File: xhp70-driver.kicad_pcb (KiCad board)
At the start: 2 copper layers, 65 x 39 mm, 13 parts, among them Q1 Q_NMOS_GDS, U1 AL8871Q

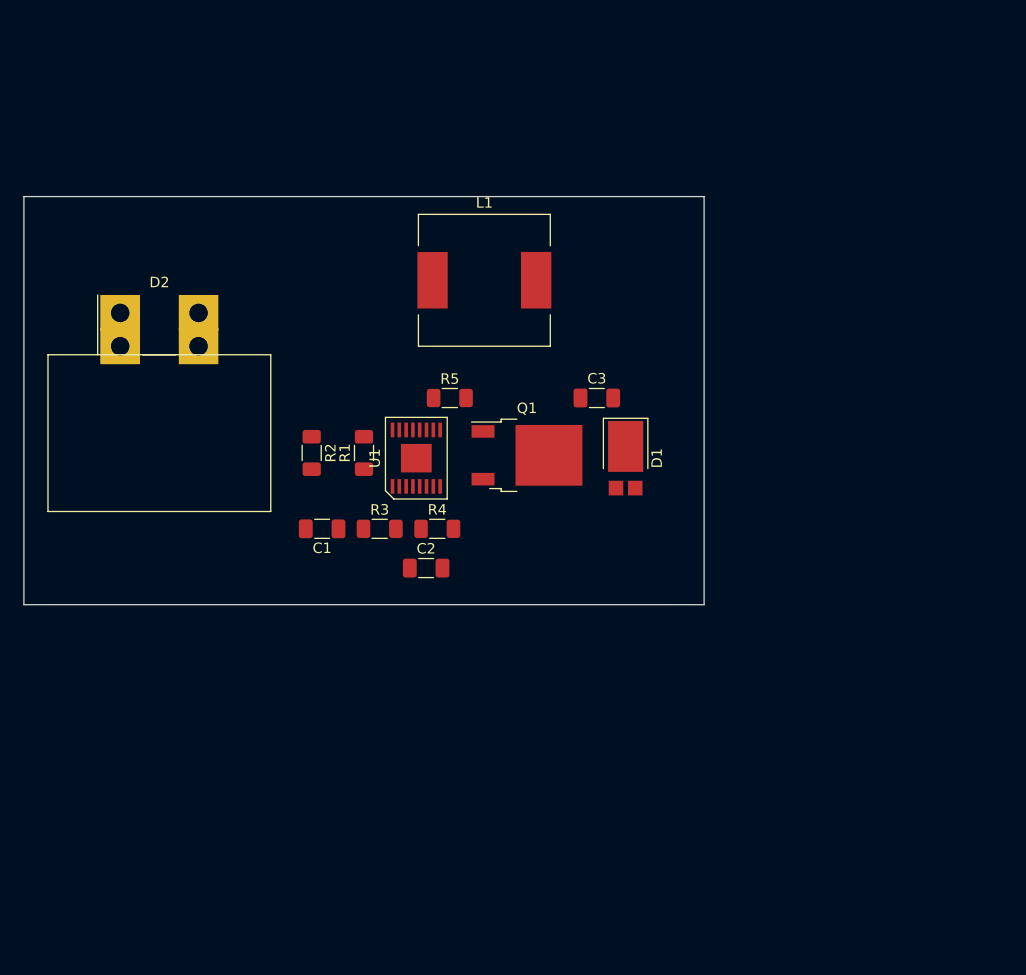
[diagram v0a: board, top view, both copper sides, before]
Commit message: Added Attiny85 MCU to control PWM of AL8871Q
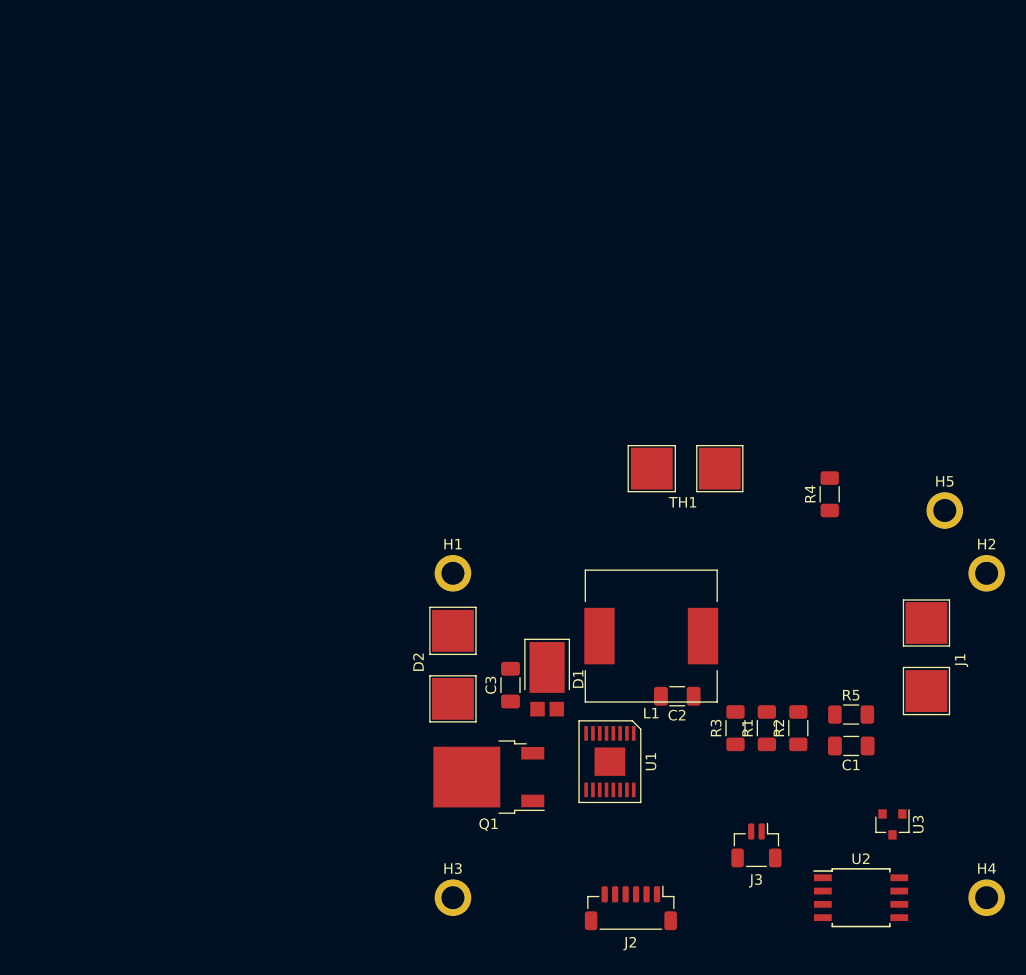
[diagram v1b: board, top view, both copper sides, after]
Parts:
- added H1: MountingHole, MountingHole:MountingHole_2.2mm_M2_ISO7380_Pad, F.Cu at (152.0, 102.0)
- added H2: MountingHole, MountingHole:MountingHole_2.2mm_M2_ISO7380_Pad, F.Cu at (203.0, 102.0)
- added H3: MountingHole, MountingHole:MountingHole_2.2mm_M2_ISO7380_Pad, F.Cu at (152.0, 133.0)
- added H4: MountingHole, MountingHole:MountingHole_2.2mm_M2_ISO7380_Pad, F.Cu at (203.0, 133.0)
- added H5: MountingHole, MountingHole:MountingHole_2.2mm_M2_ISO7380_Pad, F.Cu at (199.0, 96.0)
- added J1: LEMO2, xhp70-driver:TestPoint_2Pad_4.0x4.0mm, F.Cu at (197.0, 110.0)
- added J2: AVR-ISP-6, Connector_JST:JST_SH_BM06B-SRSS-TB_1x06-1MP_P1.00mm_Vertical, F.Cu at (169.0, 134.0)
- added J3: Conn_01x02_Male, Connector_JST:JST_SH_BM02B-SRSS-TB_1x02-1MP_P1.00mm_Vertical, F.Cu at (181.0, 128.0)
- added TH1: 10K, xhp70-driver:TestPoint_2Pad_4.0x4.0mm, F.Cu at (174.2, 91.8)
- added U2: ATtiny85-20SU, Package_SO:SOIJ-8_5.3x5.3mm_P1.27mm, F.Cu at (191.0, 133.0)
- added U3: L7805, Package_TO_SOT_SMD:SOT-23, F.Cu at (194.0, 126.0)
- D2: footprint Connector_Molex:Molex_Sabre_46007-1102_1x02_P7.49mm_Horizontal -> xhp70-driver:TestPoint_2Pad_4.0x4.0mm
- moved C1 54.7 mm to (190.1, 118.5)
- moved R2 53.4 mm to (185.0, 116.8), turned to 90 degrees
- moved R5 48.8 mm to (190.1, 115.5)
- moved R1 46.6 mm to (182.0, 116.8)
- moved D2 44.2 mm to (152.2, 110.8), turned to 90 degrees
- moved R3 39.0 mm to (179.0, 116.8), turned to 90 degrees
- moved R4 37.6 mm to (188.0, 94.5), turned to 90 degrees
- moved L1 37.6 mm to (170.9, 108.0), turned to 180 degrees
- moved U1 34.4 mm to (167.0, 120.0), turned to 180 degrees
- moved Q1 31.0 mm to (155.4, 121.5), turned to 180 degrees
- moved C3 28.7 mm to (157.5, 112.7), turned to 90 degrees
- moved C2 26.9 mm to (173.4, 113.8), turned to 180 degrees
- moved D1 22.4 mm to (161.0, 112.1)
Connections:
- net +BATT renamed Batt+
- U1 pad 15: Net-(U1-Pad15) -> PWM
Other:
- board outline removed
- net class GND added: clearance 0.2, trace_width 0.4, via_dia 0.8, via_drill 0.4
- net class LED+ added: clearance 0.2, trace_width 0.8, via_dia 0.8, via_drill 0.4

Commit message: Added components and route connections in xhp70-driver-test-route.pro file
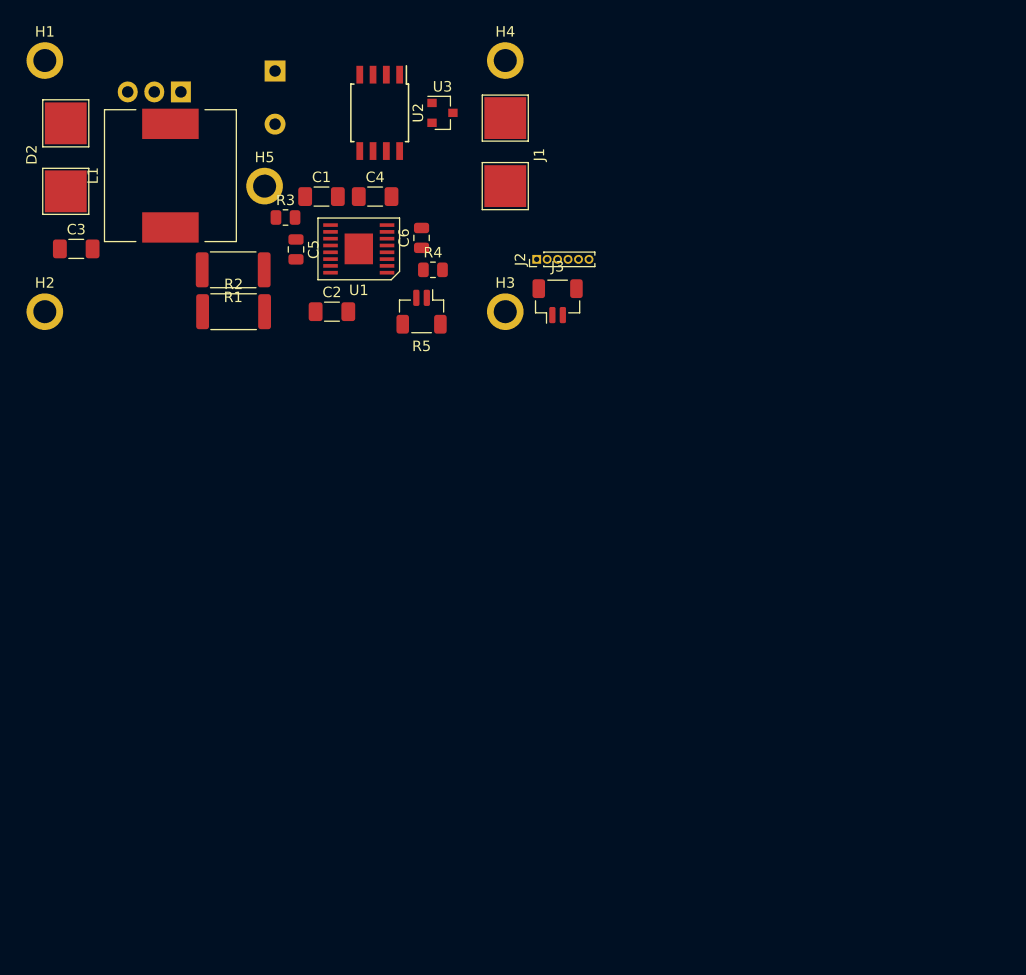
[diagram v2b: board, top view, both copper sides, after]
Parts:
- removed TH1: 10K, xhp70-driver:TestPoint_2Pad_4.0x4.0mm
- added C4: 1uF, Capacitor_SMD:C_1206_3216Metric_Pad1.33x1.80mm_HandSolder, F.Cu at (144.6, 66.0)
- added C5: 100nF, Capacitor_SMD:C_0805_2012Metric, F.Cu at (137.0, 71.0)
- added C6: 330pF, Capacitor_SMD:C_0805_2012Metric, F.Cu at (149.0, 70.0)
- C1, C2: value C -> 10uF
- C3: value C -> 1uF
- D1: value D -> D_Schottky; footprint Diode_SMD:D_PowerDI-5 -> xhp70-driver:TO-220-2_Horizontal_TabUp-no-mounting-hole; moved to B.Cu
- J2: footprint Connector_JST:JST_SH_BM06B-SRSS-TB_1x06-1MP_P1.00mm_Vertical -> Connector_PinHeader_1.00mm:PinHeader_1x06_P1.00mm_Vertical
- Q1: footprint Package_TO_SOT_SMD:TO-252-2 -> xhp70-driver:TO-220-3_Horizontal_TabUp-no-mounting-hole; moved to B.Cu
- R1: value R -> 0.09; footprint Resistor_SMD:R_1206_3216Metric_Pad1.30x1.75mm_HandSolder -> Resistor_SMD:R_2512_6332Metric
- R2: value R -> 0.082; footprint Resistor_SMD:R_1206_3216Metric_Pad1.30x1.75mm_HandSolder -> Resistor_SMD:R_2512_6332Metric
- R3: value R -> 2.2K; footprint Resistor_SMD:R_1206_3216Metric_Pad1.30x1.75mm_HandSolder -> Resistor_SMD:R_0805_2012Metric
- R4: value R -> 1.3K; footprint Resistor_SMD:R_1206_3216Metric_Pad1.30x1.75mm_HandSolder -> Resistor_SMD:R_0805_2012Metric
- R5: value R -> 10K; footprint Resistor_SMD:R_1206_3216Metric_Pad1.30x1.75mm_HandSolder -> Connector_JST:JST_SH_BM02B-SRSS-TB_1x02-1MP_P1.00mm_Vertical
- moved H2 93.4 mm to (113.0, 77.0)
- moved H4 92.3 mm to (157.0, 53.0)
- moved U2 88.0 mm to (145.0, 58.0), turned to 270 degrees
- moved U3 80.5 mm to (151.0, 58.0), turned to 0 degrees
- moved C1 72.9 mm to (139.4, 66.0), turned to 0 degrees
- moved H5 72.0 mm to (134.0, 65.0)
- moved Q1 71.8 mm to (126.0, 56.0)
- moved R1 67.2 mm to (131.0, 73.0), turned to 180 degrees
- moved R2 67.1 mm to (131.0, 77.0), turned to 0 degrees
- moved R3 65.0 mm to (136.0, 68.0), turned to 0 degrees
- moved D1 63.7 mm to (135.0, 54.0)
- moved L1 63.6 mm to (125.0, 64.0), turned to 90 degrees
- moved J1 62.8 mm to (156.8, 61.8)
- moved J2 62.6 mm to (160.0, 72.0), turned to 90 degrees
- moved H1 62.6 mm to (113.0, 53.0)
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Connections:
- C2 pad 1: Net-(C2-Pad1) -> Batt+
- C3 pad 1: Batt+ -> Net-(C3-Pad1)
- D1 pad 1: Net-(C3-Pad2) -> Batt+
- D2 pad 1: Batt+ -> Net-(C3-Pad1)
- J2 pad 1: PWM -> Net-(J2-Pad1)
- L1 pad 1: Net-(L1-Pad1) -> Net-(C3-Pad1)
- R1 pad 1: Net-(R1-Pad1) -> Batt+
- R1 pad 2: Net-(R1-Pad2) -> Net-(C3-Pad2)
- R2 pad 1: Net-(R1-Pad2) -> Batt+
- R2 pad 2: GND -> Net-(C3-Pad2)
- R3 pad 1: Net-(R1-Pad1) -> Net-(Q1-Pad1)
- R4 pad 1: Net-(R3-Pad2) -> Net-(R4-Pad1)
- R4 pad 2: GND -> Net-(R4-Pad2)
- R5 pad 1: Net-(L1-Pad1) -> Net-(R4-Pad2)
- R5 pad 2: Batt+ -> GND
- U1 pad 1: Net-(R1-Pad1) -> Net-(R4-Pad1)
- U1 pad 10: Net-(Q1-Pad1) -> Net-(R3-Pad2)
- U1 pad 11: Net-(U1-Pad11) -> Batt+
- U1 pad 13: Net-(L1-Pad1) -> Net-(C3-Pad2)
- U1 pad 16: Net-(R1-Pad2) -> Net-(R4-Pad1)
- U1 pad 2: Net-(R1-Pad1) -> Net-(R4-Pad1)
- U1 pad 3: Net-(R3-Pad2) -> Net-(R4-Pad2)
- U1 pad 4: Net-(C2-Pad1) -> Net-(C6-Pad1)
- U1 pad 8: GND -> Net-(U1-Pad8)
- U1 pad 9: Net-(Q1-Pad1) -> Net-(U1-Pad9)
- U2 pad 3: Net-(U2-Pad3) -> PWM
- U2 pad 6: PWM -> Net-(J2-Pad1)

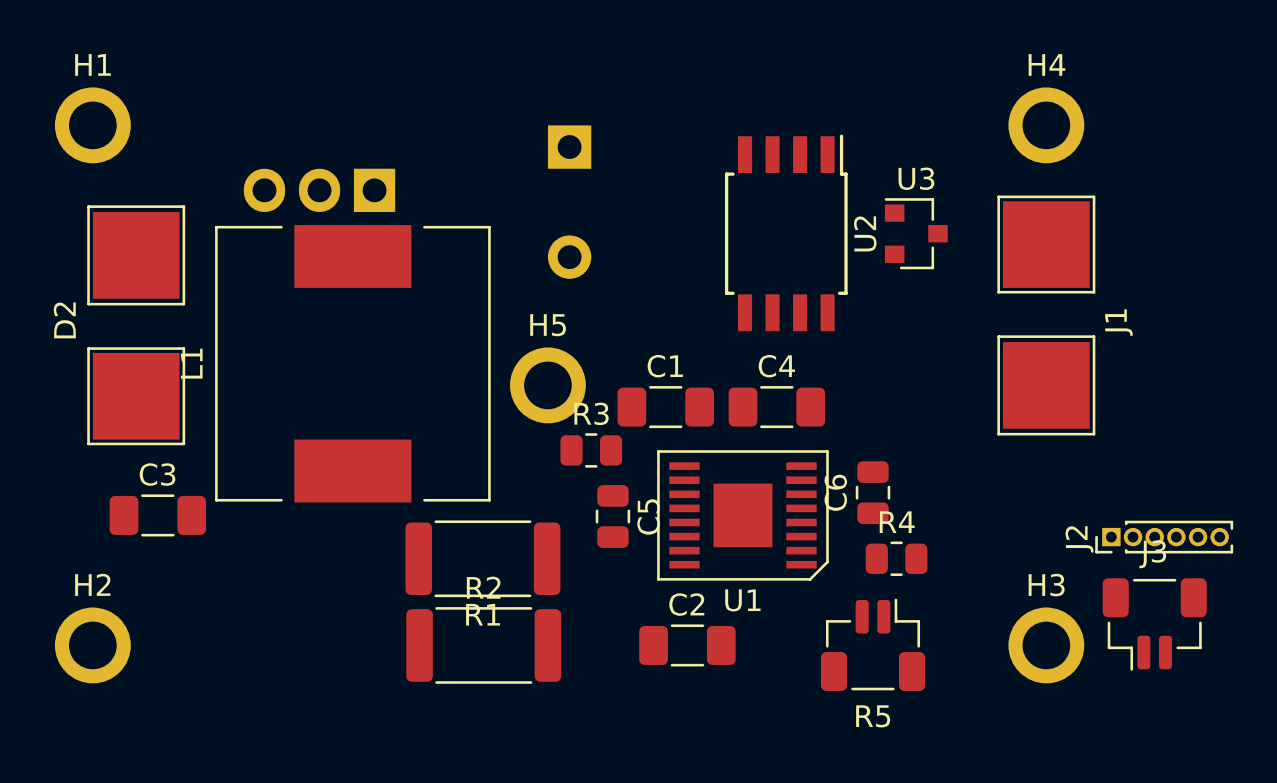
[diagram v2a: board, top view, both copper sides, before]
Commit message: Reposition and changed connector. Reroute traces
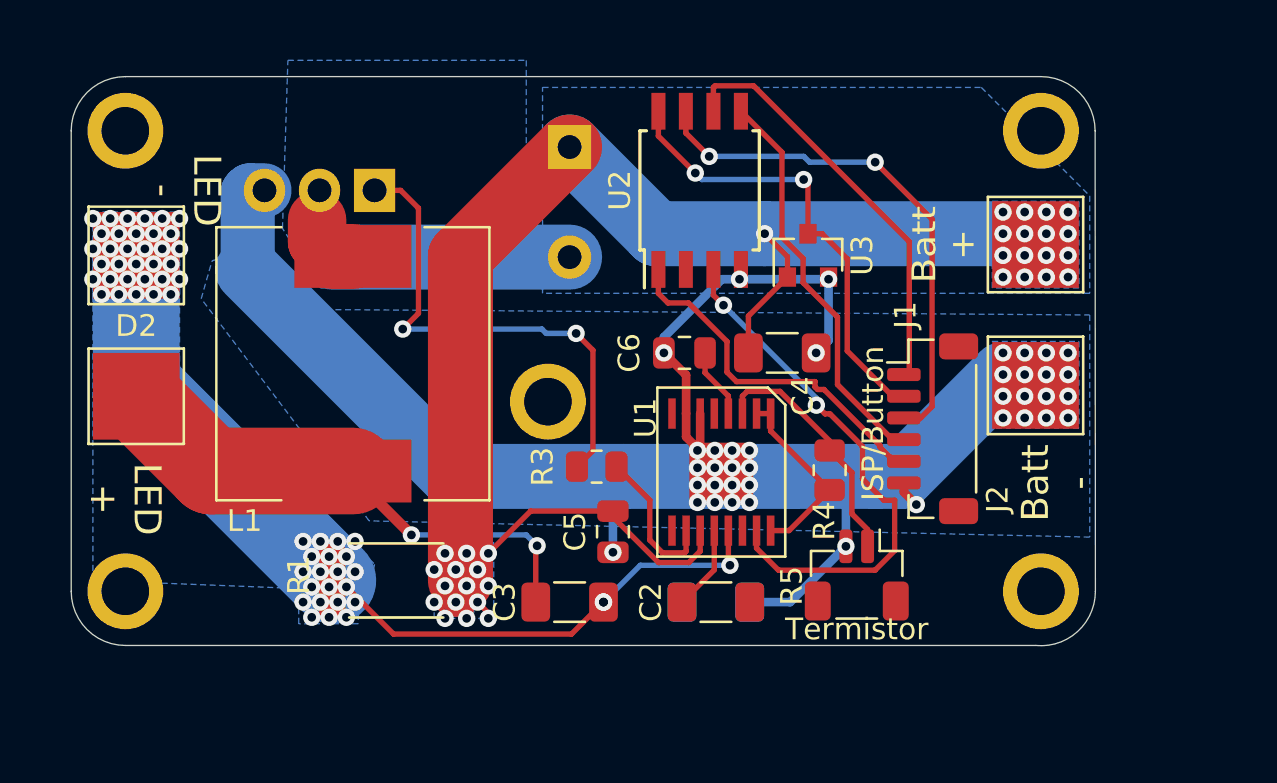
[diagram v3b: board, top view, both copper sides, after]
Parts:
- removed J3: Conn_01x02_Male, Connector_JST:JST_SH_BM02B-SRSS-TB_1x02-1MP_P1.00mm_Vertical
- C1, R2: moved to B.Cu
- J2: footprint Connector_PinHeader_1.00mm:PinHeader_1x06_P1.00mm_Vertical -> Connector_JST:JST_SH_BM06B-SRSS-TB_1x06-1MP_P1.00mm_Vertical
- moved C3 19.4 mm to (135.0, 75.0)
- moved C6 10.8 mm to (140.3, 63.5), turned to 180 degrees
- moved J2 9.65 mm to (151.8, 67.0), turned to 270 degrees
- moved C1 9.29 mm to (141.8, 75.0)
- moved R4 5.12 mm to (147.0, 68.9), turned to 90 degrees
- moved U3 5.10 mm to (146.0, 59.0), turned to 90 degrees
- moved R2 5.00 mm to (127.0, 74.0), turned to 180 degrees
- moved U2 4.47 mm to (141.0, 56.0), turned to 90 degrees
- moved R1 4.12 mm to (127.0, 74.0)
- moved R5 3.34 mm to (148.2, 73.8)
- moved H2 2.92 mm to (114.5, 74.5)
- moved C4 2.51 mm to (144.8, 63.5)
- moved H3 2.51 mm to (156.8, 74.5)
- moved C2 2.39 mm to (141.8, 75.0)
- moved U1 2.24 mm to (142.0, 69.0), turned to 180 degrees
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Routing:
- net GND: track 0.00 -> 82.1 mm, vias 0 -> 39
- net Batt+: track 0.00 -> 70.1 mm, vias 0 -> 32
- net Net-(C3-Pad2): track 0.00 -> 40.3 mm, vias 0 -> 57
- net PWM: track 0.00 -> 24.8 mm, vias 0 -> 2
- net Net-(J2-Pad3): track 0.00 -> 24.2 mm, vias 0 -> 2
- net Net-(C3-Pad1): track 0.00 -> 24.1 mm, vias 0 -> 2
- net Net-(Q1-Pad1): track 0.00 -> 23.1 mm, vias 0 -> 2
- net Net-(J2-Pad2): track 0.00 -> 21.5 mm, vias 0 -> 2
- net Net-(J2-Pad1): track 0.00 -> 19.3 mm
- net Net-(J2-Pad4): track 0.00 -> 18.8 mm
- net Net-(J2-Pad5): track 0.00 -> 17.3 mm
- net Net-(D1-Pad2): track 0.00 -> 16.1 mm
- net Net-(R4-Pad2): track 0.00 -> 11.5 mm
- net Net-(R4-Pad1): track 0.00 -> 8.81 mm
- net Net-(R3-Pad2): track 0.00 -> 6.92 mm
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- added copper zone on B.Cu, net Batt+
- added copper zone on B.Cu, net GND
- added copper zone on B.Cu, net Net-(C3-Pad2)
- added copper zone on B.Cu, net Net-(D1-Pad2)
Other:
- board outline added: 47.3 x 26.3 mm
- net class Thick added: clearance 0.2, trace_width 4, via_dia 0.8, via_drill 0.4
- board text added: "Batt +"
- board text added: "Batt -"
- board text added: "ISP/Button"
- board text added: "LED +"
- board text added: "LED -"
- board text added: "Termistor"
